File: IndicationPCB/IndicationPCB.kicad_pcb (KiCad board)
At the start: 2 copper layers, 14.5 x 63 mm, 14 parts, among them J1 Conn_01x03

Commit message: logo!
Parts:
- LOGO1: footprint UTSVT_Logos:UTSVT_Logo_Symbol -> UTSVT_Logos:LHRs_LOGO
- moved J1 2.00 mm to (148.1, 65.5)
- moved LOGO1 1.75 mm to (144.6, 82.2), turned to 90 degrees
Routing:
- net /DIN: track 16.4 -> 13.9 mm
- net +5V: track 53.9 -> 51.6 mm

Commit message: gerber
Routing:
- net /DIN: track 13.9 -> 13.6 mm, vias 0 -> 1
- added copper zone on B.Cu, net GND
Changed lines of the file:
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@@
 	)
 	(segment
-		(start 150.899 63.259)
-		(end 148.14 60.5)
+		(start 147.45 71.85)
+		(end 149.15 70.15)
 		(width 0.2)
 		(layer "F.Cu")
 		(net 3)
 	)
-	(segment
-		(start 147.45 71.85)
-		(end 150.899 68.401)
-		(width 0.2)
-		(layer "F.Cu")
+	(via
+		(at 149.15 70.15)
+		(size 0.6)
+		(drill 0.3)
+		(layers "F.Cu" "B.Cu")
 		(net 3)
 	)
 	(segment
-		(start 150.899 68.401)
-		(end 150.899 63.259)
+		(start 150.5 68.8)
+		(end 150.5 62.86)
 		(width 0.2)
-		(layer "F.Cu")
+		(layer "B.Cu")
+		(net 3)
+	)
+	(segment
+		(start 150.5 62.86)
+		(end 148.14 60.5)
+		(width 0.2)
+		(layer "B.Cu")
+		(net 3)
+	)
+	(segment
+		(start 149.15 70.15)
+		(end 150.5 68.8)
+		(width 0.2)
+		(layer "B.Cu")
 		(net 3)
 	)
@@
 		(net 2)
 		(net_name "GND")
-		(layer "F.Cu")
+		(layers "F.Cu" "B.Cu")
 		(hatch edge 0.5)
 		(connect_pads

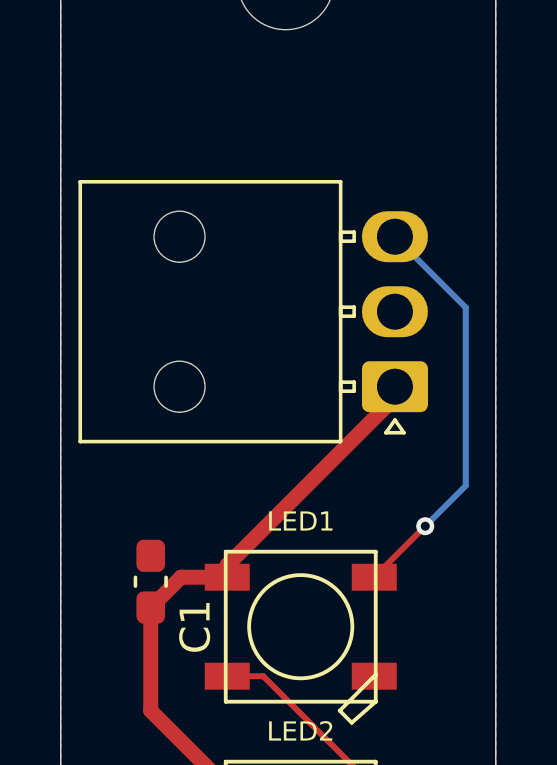
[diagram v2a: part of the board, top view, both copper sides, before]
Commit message: new connector
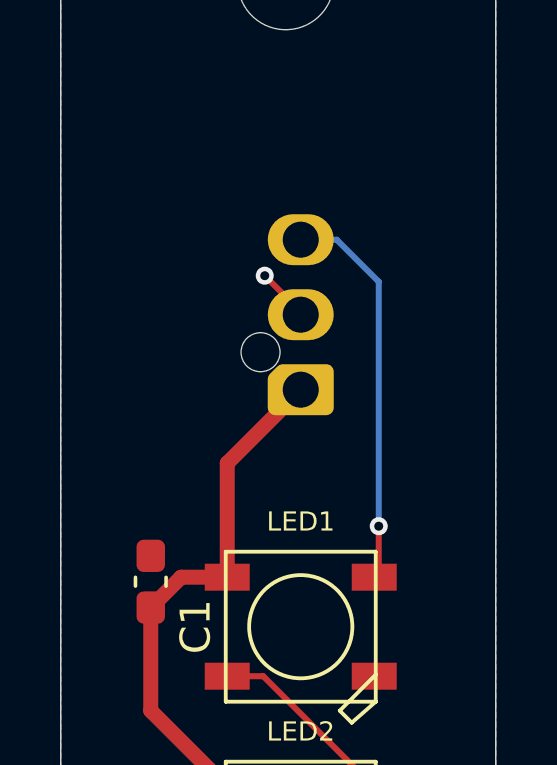
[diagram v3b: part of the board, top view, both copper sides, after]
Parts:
- J1: footprint Connector_Molex:Molex_Nano-Fit_105313-xx03_1x03_P2.50mm_Horizontal -> Connector_Molex:Molex_Nano-Fit_105309-xx03_1x03_P2.50mm_Vertical; moved to B.Cu
- moved J1 3.14 mm to (145.0, 65.6), turned to 0 degrees
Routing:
- net GND: track 0.00 -> 1.80 mm, vias 0 -> 1
- net +5V: track 51.6 -> 50.5 mm
